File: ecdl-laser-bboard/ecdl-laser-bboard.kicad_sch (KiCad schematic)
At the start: 0 parts

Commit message: started laser breakout board interconnect
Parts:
- added J1: D15S33E4GV00LF, D15S33E4GV00LF:AMPHENOL_D15S33E4GV00LF, symbol D15S33E4GV00LF:D15S33E4GV00LF
- added J2: DB9, CONN_D09S33E4GV00LF_AMP, symbol D09S33E4GV00LF:D09S33E4GV00LF
- added J3: LDTC0520_INTERFACE, symbol Connector:Conn_01x04_Pin
- added R1: 0, symbol Device:R
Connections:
- new net: J2.6, R1.1
- new net GND: J3.4 (Pin_4)
- new net J3-1: J2.4, J2.5, R1.2
- new net J3-2: J2.7
- new net J3-4: J2.8, J2.9
- new net VDD_FL: J3.1 (Pin_1)
- new net VDD_WTC: J3.2 (Pin_2)
- new net VS_TEC: J3.3 (Pin_3)
- no-connect marks 0 -> 3
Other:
- note added: "224B DB9 connector"

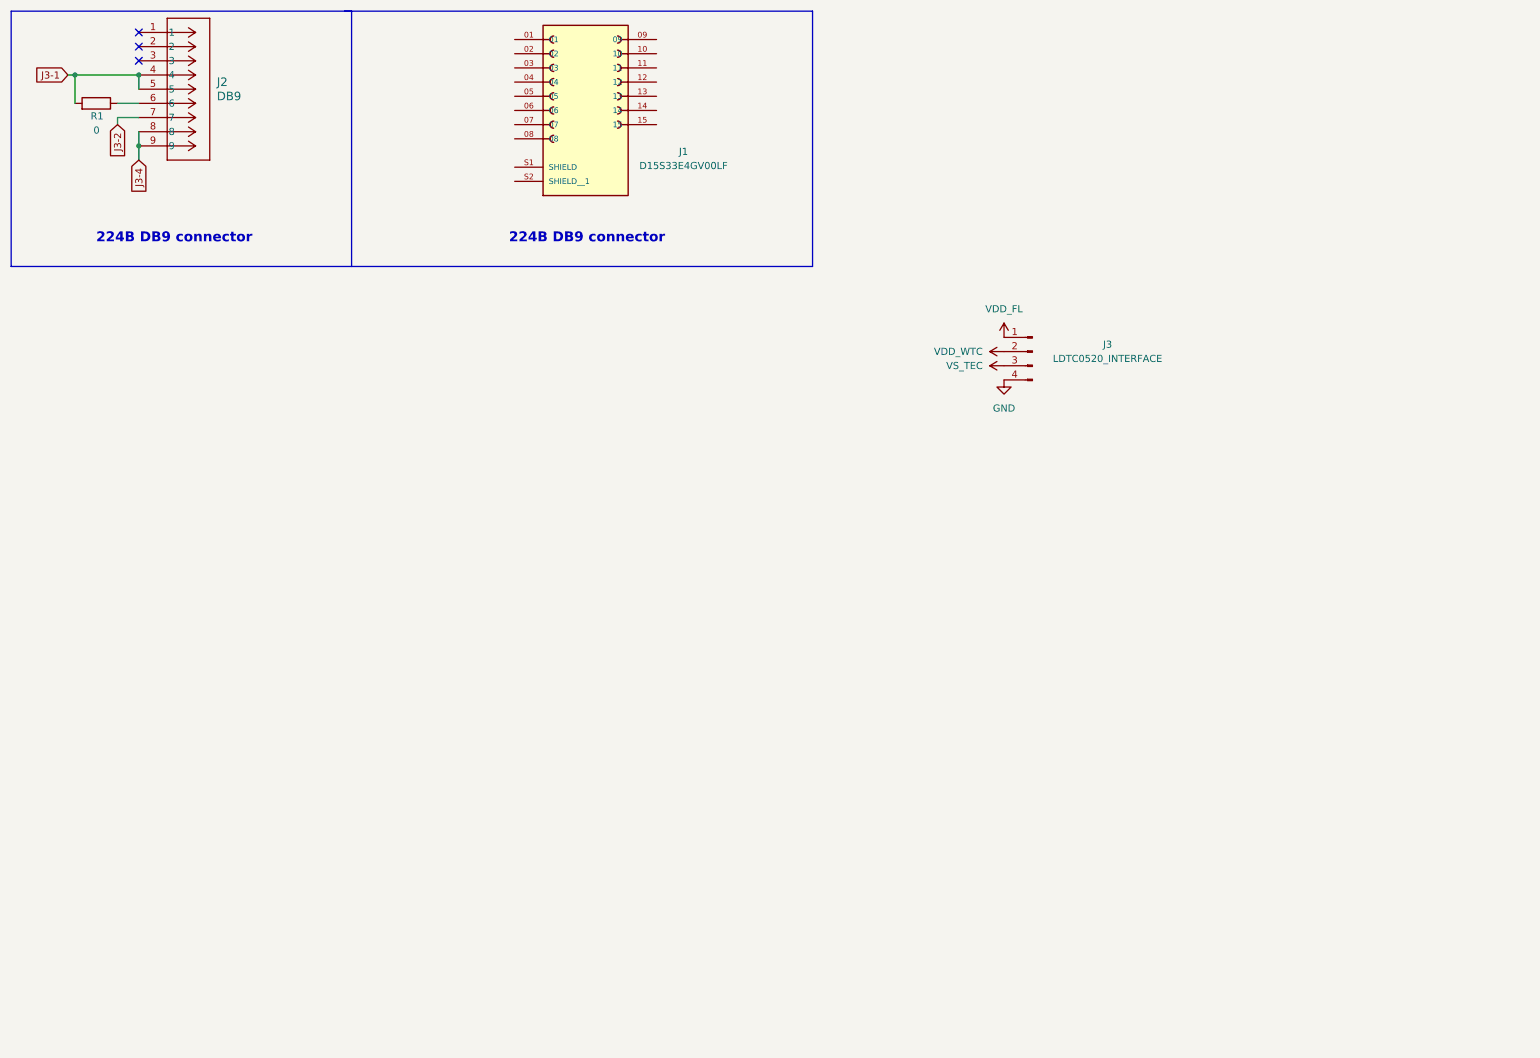
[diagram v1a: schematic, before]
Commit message: added pwr/pwr safety sections
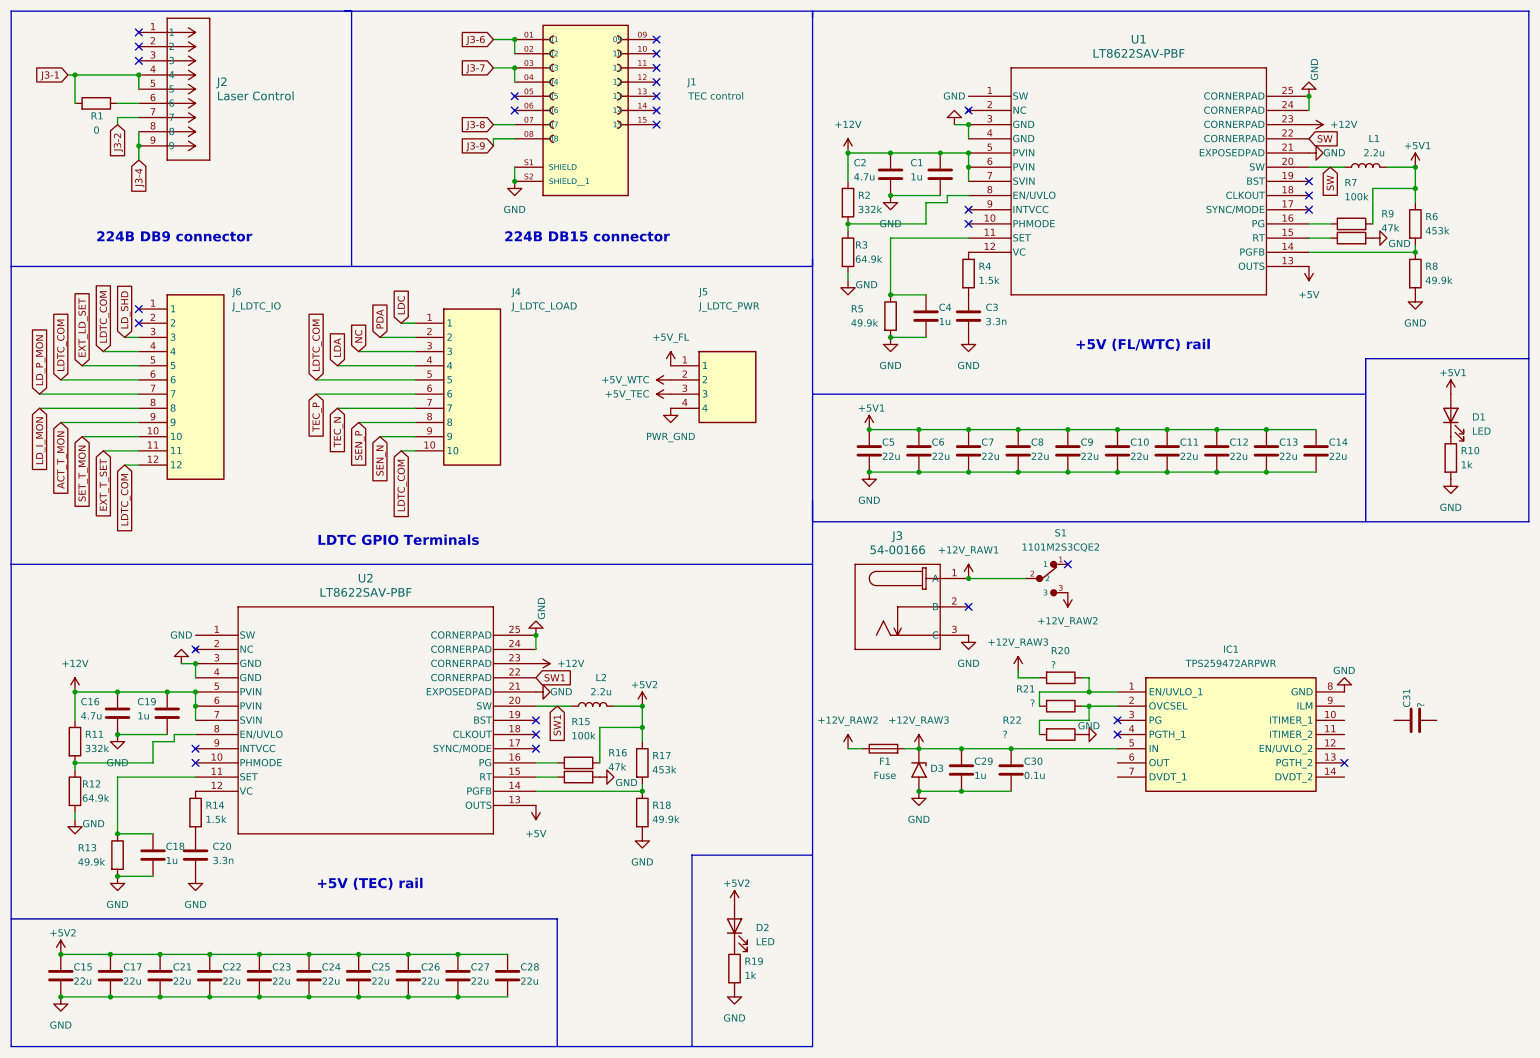
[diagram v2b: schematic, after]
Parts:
- removed J3: LDTC0520_INTERFACE, symbol Connector:Conn_01x04_Pin
- added C1, C18, C19, C29, C4: 1u, Capacitor_SMD:C_0603_1608Metric, symbol Device:C
- added C10, C11, C12, C13, C14, C15, C17, C21, C22, C23, C24, C25, C26, C27, C28, C5, C6, C7, C8, C9: 22u, Capacitor_SMD:C_0603_1608Metric, symbol Device:C
- added C16, C2: 4.7u, Capacitor_SMD:C_0603_1608Metric, symbol Device:C
- added C20, C3: 3.3n, Capacitor_SMD:C_0603_1608Metric, symbol Device:C
- added C30: 0.1u, Capacitor_SMD:C_0603_1608Metric, symbol Device:C
- added C31: ?, Capacitor_SMD:C_0603_1608Metric, symbol Device:C
- added D1, D2: LED, symbol Device:LED
- added D3: (no value), symbol Diode:SM5908
- added F1: Fuse, symbol Device:Fuse
- added IC1: TPS259472ARPWR, TPS259472ARPWR, symbol TPS259472ARPWR:TPS259472ARPWR
- added J3: 54-00166, CONN3_54-00166_TEN, symbol 54-00166:54-00166
- added J4: J_LDTC_LOAD, 1757323, symbol 1757323:1757323
- added J5: J_LDTC_PWR, 1757268, symbol 1757268:1757268
- added J6: J_LDTC_IO, 1803374, symbol 1803374:1803374
- added L1, L2: 2.2u, symbol Device:L
- added R10, R19: 1k, Resistor_SMD:R_0603_1608Metric, symbol Device:R
- added R11, R2: 332k, Resistor_SMD:R_0603_1608Metric, symbol Device:R
- added R12, R3: 64.9k, Resistor_SMD:R_0603_1608Metric, symbol Device:R
- added R13, R18, R5, R8: 49.9k, Resistor_SMD:R_0603_1608Metric, symbol Device:R
- added R14, R4: 1.5k, Resistor_SMD:R_0603_1608Metric, symbol Device:R
- added R15, R7: 100k, Resistor_SMD:R_0603_1608Metric, symbol Device:R
- added R16, R9: 47k, Resistor_SMD:R_0603_1608Metric, symbol Device:R
- added R17, R6: 453k, Resistor_SMD:R_0603_1608Metric, symbol Device:R
- added R20, R21, R22: ?, Resistor_SMD:R_0603_1608Metric, symbol Device:R
- added S1: 1101M2S3CQE2, 1101M2S3CQE2:SW_1101M2S3CQE2, symbol 1101M2S3CQE2:1101M2S3CQE2
- added U1, U2: LT8622SAV-PBF, 05-08-1602_Rev_A_ADI, symbol LT8622SAV-PBF:LT8622SAV-PBF
- J1: value D15S33E4GV00LF -> TEC control
- J2: value DB9 -> Laser Control
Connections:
- net GND: now also J1.S1 (SHIELD), J1.S2 (SHIELD__1), C1.2, C10.2, C11.2, C12.2, C13.2, C14.2, C15.2, C16.2, C17.2, C18.2, C19.2, C2.2, C20.2, C21.2, C22.2, C23.2, C24.2, C25.2, C26.2, C27.2, C28.2, C29.2, C3.2, C30.2, C4.2, C5.2, C6.2, C7.2, C8.2, C9.2, D3.2 (A2), IC1.8 (GND), J3.3 (C), R10.2, R12.2, R13.2, R16.2, R18.2, R19.2, R22.1, R3.2, R5.2, R8.2, R9.2, U1.21 (EXPOSEDPAD), U1.24 (CORNERPAD), U1.25 (CORNERPAD), U1.3 (GND), U1.4 (GND), U2.21 (EXPOSEDPAD), U2.24 (CORNERPAD), U2.25 (CORNERPAD), U2.3 (GND), U2.4 (GND)
- net J3-6: now reaches J1.01
- net J3-6: now also J1.02
- net J3-7: now reaches J1.03
- net J3-7: now also J1.04
- net J3-8: now reaches J1.07
- net J3-9: now reaches J1.08
- new net: C20.1, R14.2
- new net: R16.1, U2.15 (RT)
- new net: R2.2, R3.1, U1.8 (EN/UVLO)
- new net: IC1.1 (EN/UVLO_1), R20.1, R21.2
- new net: C4.1, R5.1, U1.11 (SET)
- new net: D1.1 (K), R10.1
- new net: C18.1, R13.1, U2.11 (SET)
- new net: C3.1, R4.2
- new net: R9.1, U1.15 (RT)
- new net: R17.2, R18.1, U2.14 (PGFB)
- new net: R11.2, R12.1, U2.8 (EN/UVLO)
- new net: R14.1, U2.12 (VC)
- new net: R7.1, U1.16 (PG)
- new net: R6.2, R8.1, U1.14 (PGFB)
- new net: D2.1 (K), R19.1
- new net: R4.1, U1.12 (VC)
- new net: R15.1, U2.16 (PG)
- new net: IC1.2 (OVCSEL), R21.1, R22.2
- new net +12V: C1.1, C16.1, C19.1, C2.1, R11.1, R2.1, U1.23 (CORNERPAD), U1.5 (PVIN), U1.6 (PVIN), U1.7 (SVIN), U2.23 (CORNERPAD), U2.5 (PVIN), U2.6 (PVIN), U2.7 (SVIN)
- new net +12V_RAW1: J3.1 (A), S1.2
- new net +12V_RAW2: F1.1, S1.3
- new net +12V_RAW3: C29.1, C30.1, D3.1 (A1), F1.2, IC1.5 (IN), R20.2
- new net +5V: U1.13 (OUTS), U2.13 (OUTS)
- new net +5V1: C10.1, C11.1, C12.1, C13.1, C14.1, C5.1, C6.1, C7.1, C8.1, C9.1, D1.2 (A), L1.2, R6.1, R7.2
- new net +5V2: C15.1, C17.1, C21.1, C22.1, C23.1, C24.1, C25.1, C26.1, C27.1, C28.1, D2.2 (A), L2.2, R15.2, R17.1
- new net +5V_FL: J5.1
- new net +5V_TEC: J5.3
- new net +5V_WTC: J5.2
- new net ACT_T_MON: J6.9
- new net EXT_LD_SET: J6.5
- new net EXT_T_SET: J6.11
- new net LDA: J4.4
- new net LDC: J4.1
- new net LDTC_COM: J4.10, J4.5, J6.12, J6.4, J6.6
- new net LD_I_MON: J6.8
- new net LD_P_MON: J6.7
- new net LD_SHD: J6.3
- new net NC: J4.3
- new net PDA: J4.2
- new net PWR_GND: J5.4
- new net SEN_N: J4.9
- new net SEN_P: J4.8
- new net SET_T_MON: J6.10
- new net SW: L1.1, U1.20 (SW), U1.22 (CORNERPAD)
- new net SW1: L2.1, U2.20 (SW), U2.22 (CORNERPAD)
- new net TEC_N: J4.7
- new net TEC_P: J4.6
- no-connect marks 3 -> 31
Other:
- note added: "+5V (FL/WTC) rail"
- note added: "+5V (TEC) rail"
- note added: "224B DB15 connector"
- note added: "LDTC GPIO Terminals"

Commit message: finished pwr section
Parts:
- removed IC1: TPS259472ARPWR, TPS259472ARPWR, symbol TPS259472ARPWR:TPS259472ARPWR
- added C32: 3.3n, Capacitor_SMD:C_0603_1608Metric, symbol Device:C
- added C33: 47u, Capacitor_SMD:C_1210_3225Metric, symbol Device:C
- added C34: 10u, Capacitor_SMD:C_0603_1608Metric, symbol Device:C
- added C35: 1u, Capacitor_SMD:C_0603_1608Metric, symbol Device:C
- added C36: 0.1u, Capacitor_SMD:C_0603_1608Metric, symbol Device:C
- added C37: 10n, Capacitor_SMD:C_0603_1608Metric, symbol Device:C
- added D4: B330A-13-F, symbol Device:D_Schottky
- added L3, L4: 0.1u, symbol Device:L
- added R23: 1.1k, Resistor_SMD:R_0603_1608Metric, symbol Device:R
- added R24, R25, R26, R27: 0, symbol Device:R
- added U3: TPS259474LRPWR, TPS259474ARPWR:IC_TPS259474ARPWR, symbol TPS259474ARPWR:TPS259474ARPWR
- C31: value ? -> 2.2n
- R20: value ? -> 470k
- R21: value ? -> 11k
- R22: value ? -> 47k
- U1, U2: value LT8622SAV-PBF -> LT8624SAV-PBF
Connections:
- net PWR_GND is gone; now on net GND: J5.4
- net +12V: now also C33.1, C34.1, C35.1, C36.1, C37.1, D4.1 (K), U3.6 (OUT)
- net +12V_RAW1: now also F1.1; no longer S1.2
- net +12V_RAW2: now also C29.1, C30.1, D3.1 (A1), R20.1, U3.5 (IN); no longer F1.1
- net +5V: now also C21.1, C22.1, C23.1, C24.1, C25.1, C26.1, C27.1, C28.1, D2.2 (A), R15.2, R17.1, L4.2, R26.2, R27.2; no longer U1.13 (OUTS), U2.13 (OUTS)
- net +5V1: now also U1.13 (OUTS), L3.1; no longer C10.1, C11.1, C12.1, C13.1, C14.1, C7.1, C8.1, C9.1, D1.2 (A), R6.1, R7.2
- net +5V2: now also U2.13 (OUTS), L4.1; no longer C21.1, C22.1, C23.1, C24.1, C25.1, C26.1, C27.1, C28.1, D2.2 (A), R15.2, R17.1
- net GND: now also C31.2, R22.2, C32.2, C33.2, C34.2, C35.2, C36.2, C37.2, D4.2 (A), R23.2, R24.1, R25.1, U3.8 (GND); no longer J1.S1 (SHIELD), J1.S2 (SHIELD__1), R22.1
- net SW: now also U1.1 (SW)
- net SW1: now also U2.1 (SW)
- net at R21.2: now also R22.1, U3.2 (OVLO); no longer R20.1
- net at C31.1: now also U3.10 (ITIMER)
- net at R21.1: now also R20.2, U3.1 (EN/UVLO); no longer R22.2
- removed net +12V_RAW3: C29.1, C30.1, D3.1 (A1), F1.2, R20.2
- net +5V_FL renamed V_FL
- net V_FL: now also C10.1, C11.1, C12.1, C13.1, C14.1, C7.1, C8.1, C9.1, D1.2 (A), R6.1, R7.2, L3.2
- net +5V_TEC: no longer names the net of J5.3
- net +5V_TEC: now also R27.1
- net +5V_WTC: no longer names the net of J5.2
- net +5V_WTC: now also R26.1
- new net: F1.2, S1.2
- new net: C32.1, U3.7 (DVDT)
- new net: R23.1, U3.9 (ILM)
- new net CHASSIS: J1.S1 (SHIELD), J1.S2 (SHIELD__1), R24.2, R25.2
- no-connect marks 31 -> 30
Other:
- added sheet sch2 (sch2.kicad_sch)
- note added: "+12V INPUT"
- note added: "10.9 V < V_IN < 13.5 V"
- note added: "V_FL"
- note added: "V_TEC"
- note added: "V_WTC"
- note added: "eFuse protection circuit"
- moved on the sheet: C10, C11, C12, C13, C14, C21, C22, C23, C24, C25, C26, C27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

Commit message: saving progress before Chipotle lol
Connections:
- net NC: no longer names the net of J4.3
- no-connect marks 30 -> 31
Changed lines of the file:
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@@
+	)
+	(no_connect
+		(at 261.62 121.92)
 	)
 	(no_connect
@@
 		(pts
 			(xy 24.13 147.32) (xy 24.13 148.59)
-		)
-		(stroke
-			(width 0)
-			(type default)
-		)
-	)
-	(wire
-		(pts
-			(xy 251.46 121.92) (xy 261.62 121.92)
 		)
 		(stroke
@@
 			(hide yes)
 			(show_name no)
-			(do_not_autoplace no)
-			(effects
-				(font
-					(size 1.27 1.27)
-				)
-				(justify left)
-			)
-		)
-	)
-	(global_label "NC"
-		(shape input)
-		(at 251.46 121.92 90)
-		(fields_autoplaced yes)
-		(effects
-			(font
-				(size 1.27 1.27)
-			)
-			(justify left)
-		)
-		(property "Intersheetrefs" "${INTERSHEET_REFS}"
-			(at 251.46 116.3343 90)
-			(hide yes)
-			(show_name no)

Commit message: post chipotle GPIO progress
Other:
- added sheet sch3 (sch3.kicad_sch)
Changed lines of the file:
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@@
+		)
+	)
+	(sheet
+		(at -269.24 -11.43)
+		(size 102.87 232.41)
+		(exclude_from_sim no)
+		(in_bom yes)
+		(on_board yes)
+		(dnp no)
+		(fields_autoplaced yes)
+		(stroke
+			(width 0.1524)
+			(type solid)
+		)
+		(fill
+			(color 0 0 0 0)
+		)
+		(property "Sheetname" "sch3"
+			(at -269.24 -12.1416 0)
+			(show_name no)
+			(do_not_autoplace no)
+			(effects
+				(font
+					(size 1.27 1.27)
+				)
+				(justify left bottom)
+			)
+		)
+		(property "Sheetfile" "sch3.kicad_sch"
+			(at -269.24 221.5646 0)
+			(show_name no)
+			(do_not_autoplace no)
+			(effects
+				(font
+					(size 1.27 1.27)
+				)
+				(justify left top)
+			)
+		)
+		(instances
+			(project "ecdl-laser-bboard"
+				(path "/a8ed137d-46ee-4955-b86c-bc6ff0698adf"
+					(page "3")
+				)
+			)
 		)
 	)

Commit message: begun layout
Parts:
- added TP1: +5V, TestPoint:TestPoint_Keystone_5015_Micro_Mini, symbol Connector:TestPoint
- added TP2: V_FL, TestPoint:TestPoint_Keystone_5015_Micro_Mini, symbol Connector:TestPoint
- added TP3: +12V, TestPoint:TestPoint_Keystone_5015_Micro_Mini, symbol Connector:TestPoint
- C10, C11, C12, C13, C14, C15, C17, C21, C22, C23, C24, C25, C26, C27, C28, C5, C7, C8, C9: footprint Capacitor_SMD:C_0603_1608Metric -> Capacitor_SMD:C_1210_3225Metric
- D1, D2: footprint (none) -> LED_SMD:LED_0603_1608Metric
- D3: footprint (none) -> Diode_SMD:D_SMB
- D4: footprint (none) -> Diode_SMD:D_SMA
- F1: footprint (none) -> 0452003.MRL:FUSC6127X294N
- J2: footprint CONN_D09S33E4GV00LF_AMP -> ul_D09S33E4GV00LF:CONN_D09S33E4GV00LF_AMP
- J3: footprint CONN3_54-00166_TEN -> 54-00166:CONN3_54-00166_TEN
- J4: footprint 1757323 -> 1757323:1757323
- J5: footprint 1757268 -> 1757268:1757268
- J6: footprint 1803374 -> 1803374:1803374
- L1, L2, L3, L4: footprint (none) -> XEL6030-222MEC:XEL6030222MEC
- R1, R25: value 0 -> 0 (DNP); footprint (none) -> Resistor_SMD:R_0805_2012Metric
- R10, R19: footprint Resistor_SMD:R_0603_1608Metric -> Resistor_SMD:R_0805_2012Metric
- R24, R26, R27: footprint (none) -> Resistor_SMD:R_0805_2012Metric
- U1, U2: footprint 05-08-1602_Rev_A_ADI -> LT8622:05-08-1602_Rev_A_ADI
- U3: footprint TPS259474ARPWR:IC_TPS259474ARPWR -> TPS259474:IC_TPS259474ARPWR
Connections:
- net J3-1 is gone; now on net LDC: J2.4, J2.5, R1.2
- net J3-2 is gone; now on net PDA: J2.7
- net J3-4 is gone; now on net LDA: J2.8, J2.9
- net J3-6 is gone; now on net TEC_P: J1.01, J1.02
- net J3-7 is gone; now on net TEC_N: J1.03, J1.04
- net J3-8 is gone; now on net SEN_P: J1.07
- net J3-9 is gone; now on net SEN_N: J1.08
- net +12V: now also TP3.1
- net +5V: now also U2.13 (OUTS), TP1.1
- net +5V1: no longer U1.13 (OUTS)
- net +5V2: no longer U2.13 (OUTS)
- net CHASSIS: now also R24.1; no longer R24.2, R25.2
- net GND: now also R24.2; no longer R24.1
- net LDTC_COM: now also R25.2
- net V_FL: now also U1.13 (OUTS), TP2.1
